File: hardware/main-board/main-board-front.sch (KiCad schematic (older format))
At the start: 25 parts, among them J5 Meter Probe, J6 Footswitch, J7 USB_A, Q1 BSS138, Q2 BSS138, Q3 BSS138, U10 USBLC6-2SC6, U11 STMPS2141, U12 USBLC6-2SC6, U9 P82B96

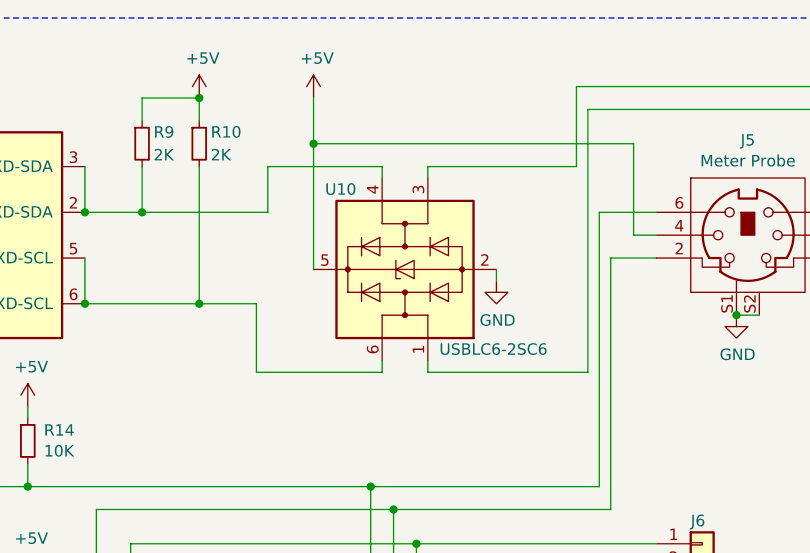
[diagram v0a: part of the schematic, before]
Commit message: First pass at doing PCB layout, all nets connected and DRC passes
Setup design rules based on a JLCPCB 4-layer board, taking initial
defaults from a combination of previous settings and various
example/template projects.

Placed all panel-mount components in dimensionally accurate locations,
and locked their footprints. These locations are based on their
datasheets and mockups of the device case panels.

Placed, arranged, and routed all PCB components. This is a first pass at
routing, so there is definitely room for tweaking and improvement.
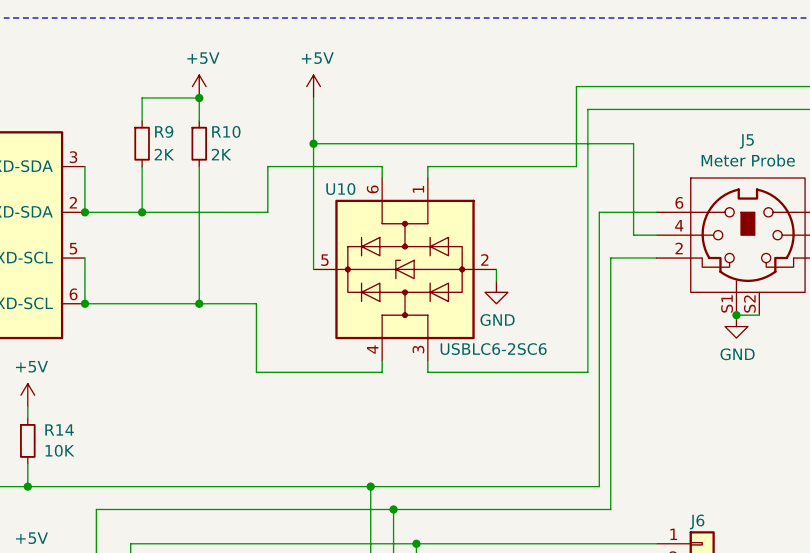
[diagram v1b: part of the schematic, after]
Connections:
- net at U10.1 (I/O1): now also J5.1; no longer J5.5
- net at U10.3 (I/O2): now also J5.5; no longer J5.1
- net at R9.2, U9.2 (RXD-SDA), U9.3 (TXD-SDA): now also U10.6 (I/O1); no longer U10.4 (I/O2)
- net at R10.2, U9.5 (TXD-SCL), U9.6 (RXD-SCL): now also U10.4 (I/O2); no longer U10.6 (I/O1)
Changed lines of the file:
@@
 AR Path="/5F9E0AB3" Ref="U?"  Part="1"
 AR Path="/5FA19AFF/5F9E0AB3" Ref="U10"  Part="1"
-F 0 "U10" V 5400 2050 50  0000 R CNN
-F 1 "USBLC6-2SC6" V 4700 1550 50  0000 R CNN
+F 0 "U10" V 4700 2050 50  0000 R CNN
+F 1 "USBLC6-2SC6" V 5400 1550 50  0000 R CNN
 F 2 "Package_TO_SOT_SMD:SOT-23-6" H 5050 1200 50  0001 C CNN
 F 3 "https://www.st.com/resource/en/datasheet/usblc6-2.pdf" H 5250 2050 50  0001 C CNN
@@
 F 8 "497-5235-1-ND" H 5050 1700 50  0001 C CNN "Supplier PN"
 	1    5050 1700
-	0    -1   -1   0
+	0    -1   1    0
 $EndComp
 Wire Wire Line

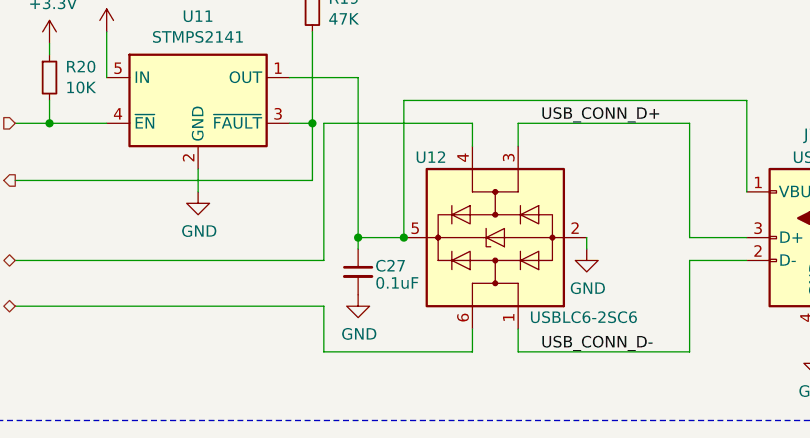
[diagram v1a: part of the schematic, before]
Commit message: PCB layout cleanup and minor fixes
Tweaked traces all over the PCB
Increased size of capacitor on USB VBUS
Added ground connections to the crystal case
Slightly increased the size of the isolated ground around the crystal
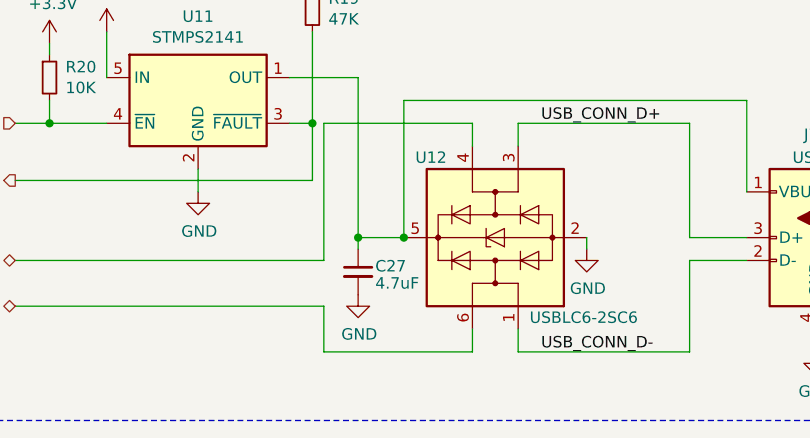
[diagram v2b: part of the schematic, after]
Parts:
- C27: value 0.1uF -> 4.7uF; footprint Capacitor_SMD:C_0603_1608Metric -> Capacitor_SMD:C_0805_2012Metric; Description CAP CER 0.1UF 25V X7R 0603 -> CAP CER 4.7UF 50V X7S 0805; Manufacturer Samsung Electro-Mechanics -> Murata Electronics; Manufacturer PN CL10B104KA8NNNC -> GRM21BC71H475KE11L; Supplier PN 1276-1006-1-ND -> 490-12757-1-ND
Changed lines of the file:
@@
 P 2850 6300
 F 0 "C27" H 2925 6325 50  0000 L CNN
-F 1 "0.1uF" H 2925 6250 50  0000 L CNN
-F 2 "Capacitor_SMD:C_0603_1608Metric" H 2850 6300 50  0001 C CNN
-F 3 "https://media.digikey.com/pdf/Data%20Sheets/Samsung%20PDFs/CL_Series_MLCC_ds.pdf" H 2850 6300 50  0001 C CNN
-F 4 "CAP CER 0.1UF 25V X7R 0603" H 2850 6300 50  0001 C CNN "Description"
-F 5 "Samsung Electro-Mechanics" H 2850 6300 50  0001 C CNN "Manufacturer"
-F 6 "CL10B104KA8NNNC" H 2850 6300 50  0001 C CNN "Manufacturer PN"
+F 1 "4.7uF" H 2925 6250 50  0000 L CNN
+F 2 "Capacitor_SMD:C_0805_2012Metric" H 2850 6300 50  0001 C CNN
+F 3 "https://search.murata.co.jp/Ceramy/image/img/A01X/G101/ENG/GRM21BC71H475KE11-01.pdf" H 2850 6300 50  0001 C CNN
+F 4 "CAP CER 4.7UF 50V X7S 0805" H 2850 6300 50  0001 C CNN "Description"
+F 5 "Murata Electronics" H 2850 6300 50  0001 C CNN "Manufacturer"
+F 6 "GRM21BC71H475KE11L" H 2850 6300 50  0001 C CNN "Manufacturer PN"
 F 7 "Digi-Key" H 2850 6300 50  0001 C CNN "Supplier"
-F 8 "1276-1006-1-ND" H 2850 6300 50  0001 C CNN "Supplier PN"
+F 8 "490-12757-1-ND" H 2850 6300 50  0001 C CNN "Supplier PN"
 	1    2850 6300
 	1    0    0    -1

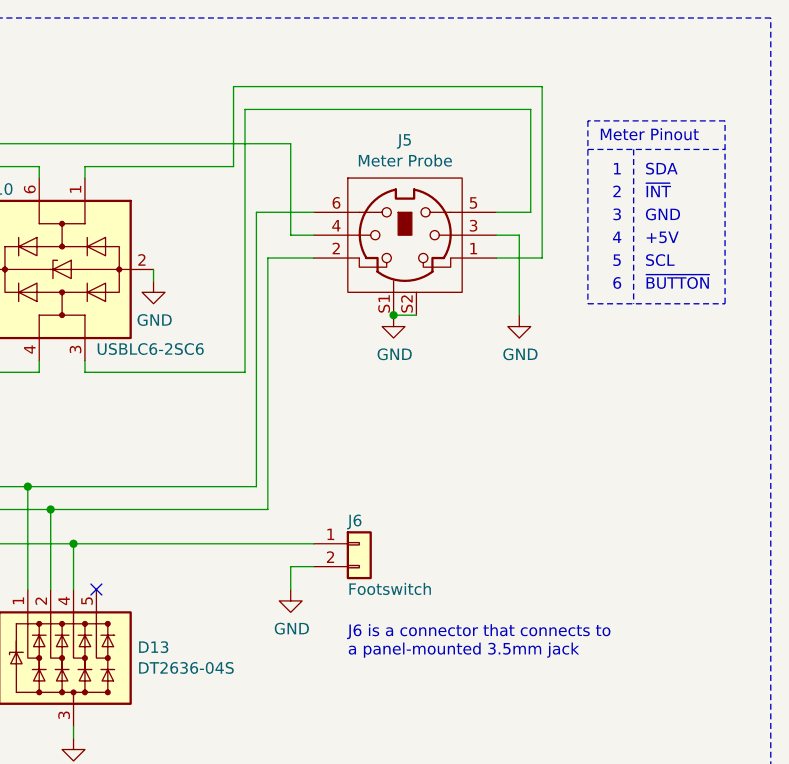
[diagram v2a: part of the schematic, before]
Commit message: Added "User Label" field to clean up BOM data for labeled common parts
This change is to prevent things like buttons, connectors, and relays
from being ungrouped on the BOM.
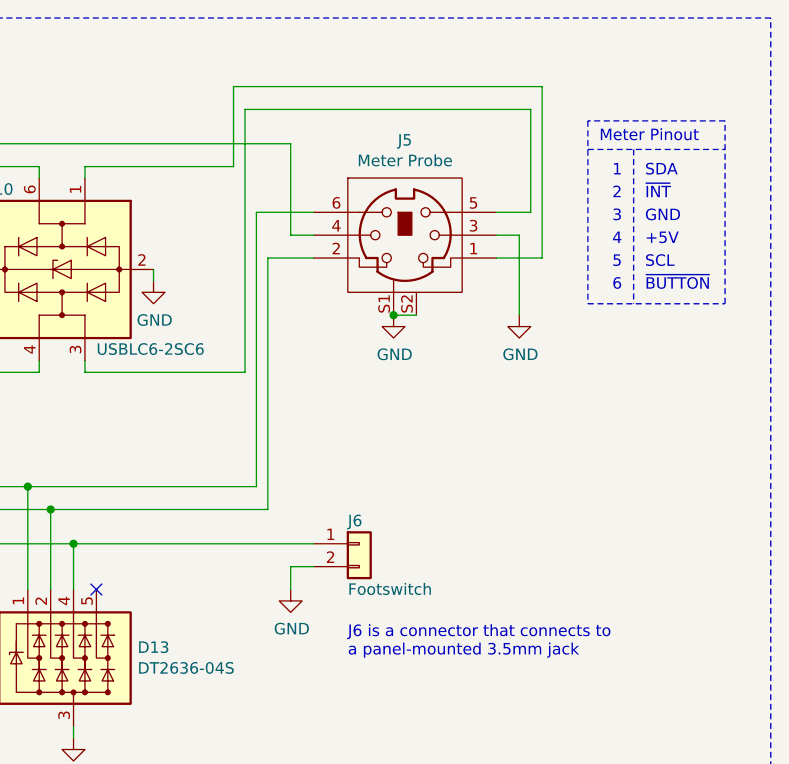
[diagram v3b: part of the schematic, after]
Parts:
- J5: value Meter Probe -> Mini-DIN 6-pin; User Label (none) -> Meter Probe
- J6: value Footswitch -> Conn_01x02; User Label (none) -> Footswitch
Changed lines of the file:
@@
 AR Path="/5FA19AFF/5FA4F940" Ref="J5"  Part="1"
 F 0 "J5" H 6550 1965 50  0000 C CNN
-F 1 "Meter Probe" H 6550 1874 50  0000 C CNN
+F 1 "Mini-DIN 6-pin" H 6550 1874 50  0001 C CNN
 F 2 "lib_fp:CUI_MD-60SM" H 6550 950 50  0001 C CNN
 F 3 "https://www.cuidevices.com/product/resource/digikeypdf/md-sm-series.pdf" H 6550 1550 50  0001 C CNN
-F 4 "CONN RCPT FMALE MINI DIN 6P SLDR" H 6550 1550 50  0001 C CNN "Description"
-F 5 "CUI Devices" H 6550 1550 50  0001 C CNN "Manufacturer"
-F 6 "MD-60SM" H 6550 1550 50  0001 C CNN "Manufacturer PN"
-F 7 "Digi-Key" H 6550 1550 50  0001 C CNN "Supplier"
-F 8 "CP-2260-ND" H 6550 1550 50  0001 C CNN "Supplier PN"
+F 4 "Meter Probe" H 6550 1875 50  0000 C CNN "User Label"
+F 5 "CONN RCPT FMALE MINI DIN 6P SLDR" H 6550 1550 50  0001 C CNN "Description"
+F 6 "CUI Devices" H 6550 1550 50  0001 C CNN "Manufacturer"
+F 7 "MD-60SM" H 6550 1550 50  0001 C CNN "Manufacturer PN"
+F 8 "Digi-Key" H 6550 1550 50  0001 C CNN "Supplier"
+F 9 "CP-2260-ND" H 6550 1550 50  0001 C CNN "Supplier PN"
 	1    6550 1550
 	1    0    0    -1
@@
 P 6350 2900
 F 0 "J6" H 6300 3000 50  0000 L CNN
-F 1 "Footswitch" H 6300 2700 50  0000 L CNN
+F 1 "Conn_01x02" H 6300 2700 50  0001 L CNN
 F 2 "Connector_JST:JST_PH_B2B-PH-K_1x02_P2.00mm_Vertical" H 6350 2900 50  0001 C CNN
 F 3 "http://www.jst-mfg.com/product/pdf/eng/ePH.pdf" H 6350 2900 50  0001 C CNN
-F 4 "CONN HEADER VERT 2POS 2MM" H 6350 2900 50  0001 C CNN "Description"
-F 5 "JST Sales America Inc." H 6350 2900 50  0001 C CNN "Manufacturer"
-F 6 "B2B-PH-K-S(LF)(SN)" H 6350 2900 50  0001 C CNN "Manufacturer PN"
-F 7 "Digi-Key" H 6350 2900 50  0001 C CNN "Supplier"
-F 8 "455-1704-ND" H 6350 2900 50  0001 C CNN "Supplier PN"
+F 4 "Footswitch" H 6300 2700 50  0000 L CNN "User Label"
+F 5 "CONN HEADER VERT 2POS 2MM" H 6350 2900 50  0001 C CNN "Description"
+F 6 "JST Sales America Inc." H 6350 2900 50  0001 C CNN "Manufacturer"
+F 7 "B2B-PH-K-S(LF)(SN)" H 6350 2900 50  0001 C CNN "Manufacturer PN"
+F 8 "Digi-Key" H 6350 2900 50  0001 C CNN "Supplier"
+F 9 "455-1704-ND" H 6350 2900 50  0001 C CNN "Supplier PN"
 	1    6350 2900
 	1    0    0    -1
